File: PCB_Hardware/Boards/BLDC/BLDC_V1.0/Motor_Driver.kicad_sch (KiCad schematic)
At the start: 27 parts, among them J10 Conn_01x03_Pin, Q3 TPH3R70APL, Q4 TPH3R70APL, Q5 TPH3R70APL, Q6 TPH3R70APL, Q7 TPH3R70APL, Q8 TPH3R70APL, U1 DRV8353SRTAR

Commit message: Add DBcan transport refactor, BLDC V1.0 schematic + sim work, HAL submodule
- DBcan: replace bare-register driver with vendor-agnostic transport abstraction (core/, transports/, refactored bootloader driver, README)
- Add stm32g4xx_hal_driver as Firmware/libs submodule
- Add HAL config for BLDC board (stm32g4xx_hal_conf.h)
- BLDC V1.0: schematic edits across 10 sheets (footprint assignments, repositioning); design-doc README (gate-driver constraints, FET selection / TPH3R70APL, thermal analysis)
- ngspice simulation workflow (cap sweeps, half-bridge slow turn-on)
- Ignore .obsidian/ vault state and large simulation CSV exports
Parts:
- C15, C16: footprint (none) -> Capacitor_SMD:C_0603_1608Metric
- C17, C18, C19, C20, C21: footprint (none) -> Capacitor_SMD:C_0402_1005Metric
- C22, C25, C26, C27, C28: footprint (none) -> Capacitor_SMD:C_0805_2012Metric
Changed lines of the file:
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@@
 			)
 		)
-		(property "Footprint" ""
+		(property "Footprint" "Capacitor_SMD:C_0805_2012Metric"
 			(at 191.4652 40.64 0)
 			(hide yes)
@@
 			)
 		)
-		(property "Footprint" ""
+		(property "Footprint" "Capacitor_SMD:C_0603_1608Metric"
 			(at 110.1852 67.31 0)
 			(hide yes)
@@
 			)
 		)
-		(property "Footprint" ""
+		(property "Footprint" "Capacitor_SMD:C_0402_1005Metric"
 			(at 80.9752 97.79 0)
 			(hide yes)
@@
 			)
 		)
-		(property "Footprint" ""
+		(property "Footprint" "Capacitor_SMD:C_0402_1005Metric"
 			(at 135.5852 175.26 0)
 			(hide yes)
@@
 			)
 		)
-		(property "Footprint" ""
+		(property "Footprint" "Capacitor_SMD:C_0805_2012Metric"
 			(at 166.0652 40.64 0)
 			(hide yes)
@@
 			)
 		)
-		(property "Footprint" ""
+		(property "Footprint" "Capacitor_SMD:C_0805_2012Metric"
 			(at 153.3652 40.64 0)
 			(hide yes)
@@
 			)
 		)
-		(property "Footprint" ""
+		(property "Footprint" "Capacitor_SMD:C_0402_1005Metric"
 			(at 149.5552 175.26 0)
 			(hide yes)
@@
 			)
 		)
-		(property "Footprint" ""
+		(property "Footprint" "Capacitor_SMD:C_0603_1608Metric"
 			(at 110.1852 81.28 0)
 			(hide yes)
@@
 			)
 		)
-		(property "Footprint" ""
+		(property "Footprint" "Capacitor_SMD:C_0805_2012Metric"
 			(at 140.6652 40.64 0)
 			(hide yes)
@@
 			)
 		)
-		(property "Footprint" ""
+		(property "Footprint" "Capacitor_SMD:C_0805_2012Metric"
 			(at 178.7652 40.64 0)
 			(hide yes)
@@
 			)
 		)
-		(property "Footprint" ""
+		(property "Footprint" "Capacitor_SMD:C_0402_1005Metric"
 			(at 97.4852 64.77 0)
 			(hide yes)
@@
 			)
 		)
-		(property "Footprint" ""
+		(property "Footprint" "Capacitor_SMD:C_0402_1005Metric"
 			(at 92.4052 97.79 0)
 			(hide yes)

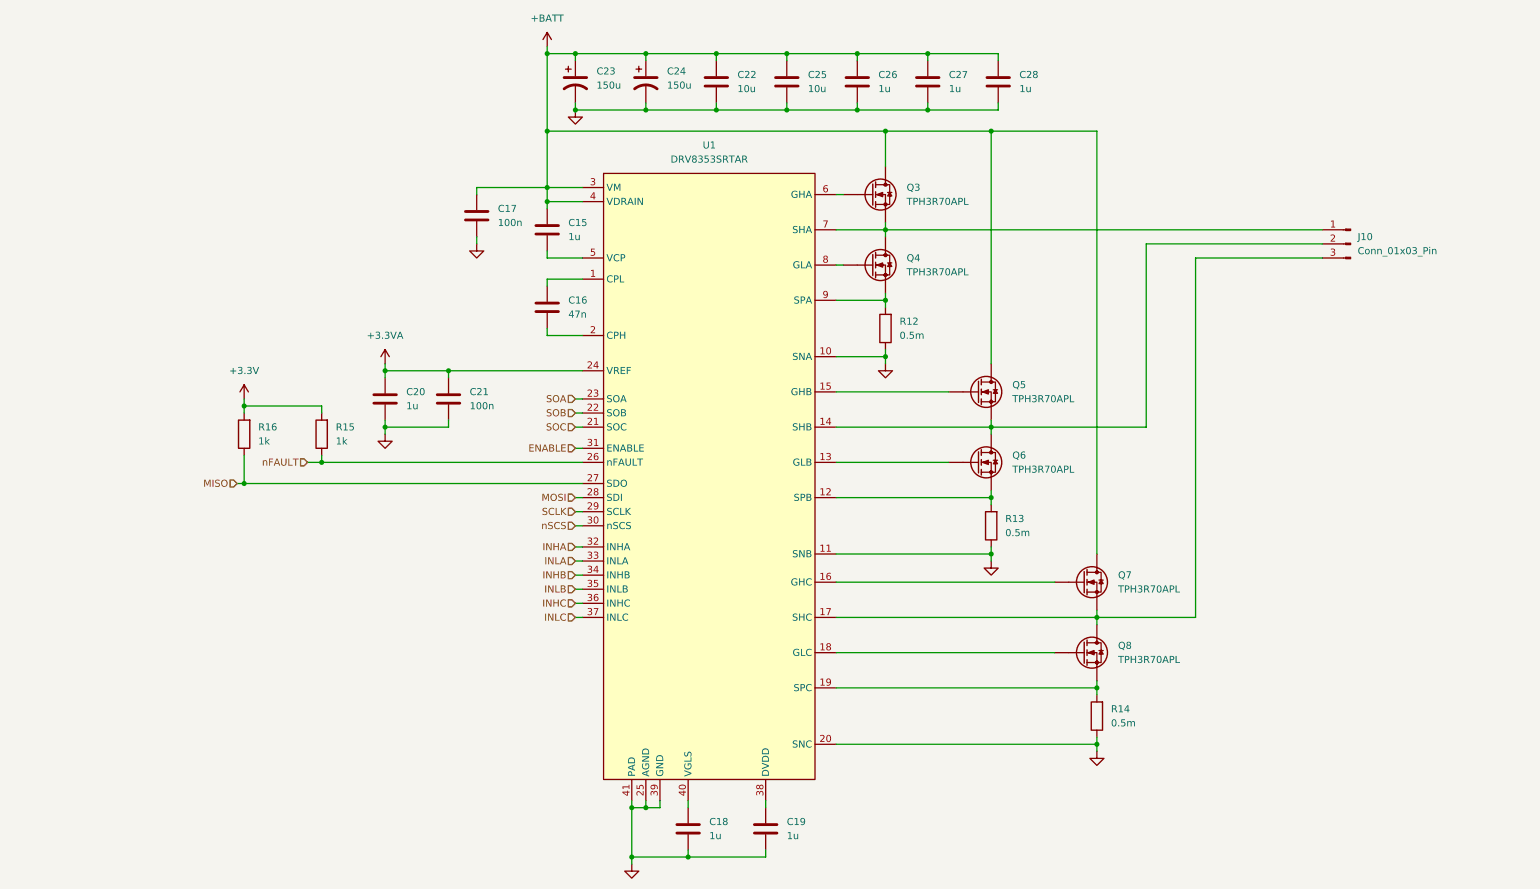
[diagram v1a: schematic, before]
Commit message: migrated claude skills to opencode, and added to the schematic review skill. Also updated the readme with calculations for the BLDC driver and changed the sense resistors to 1m Ohm
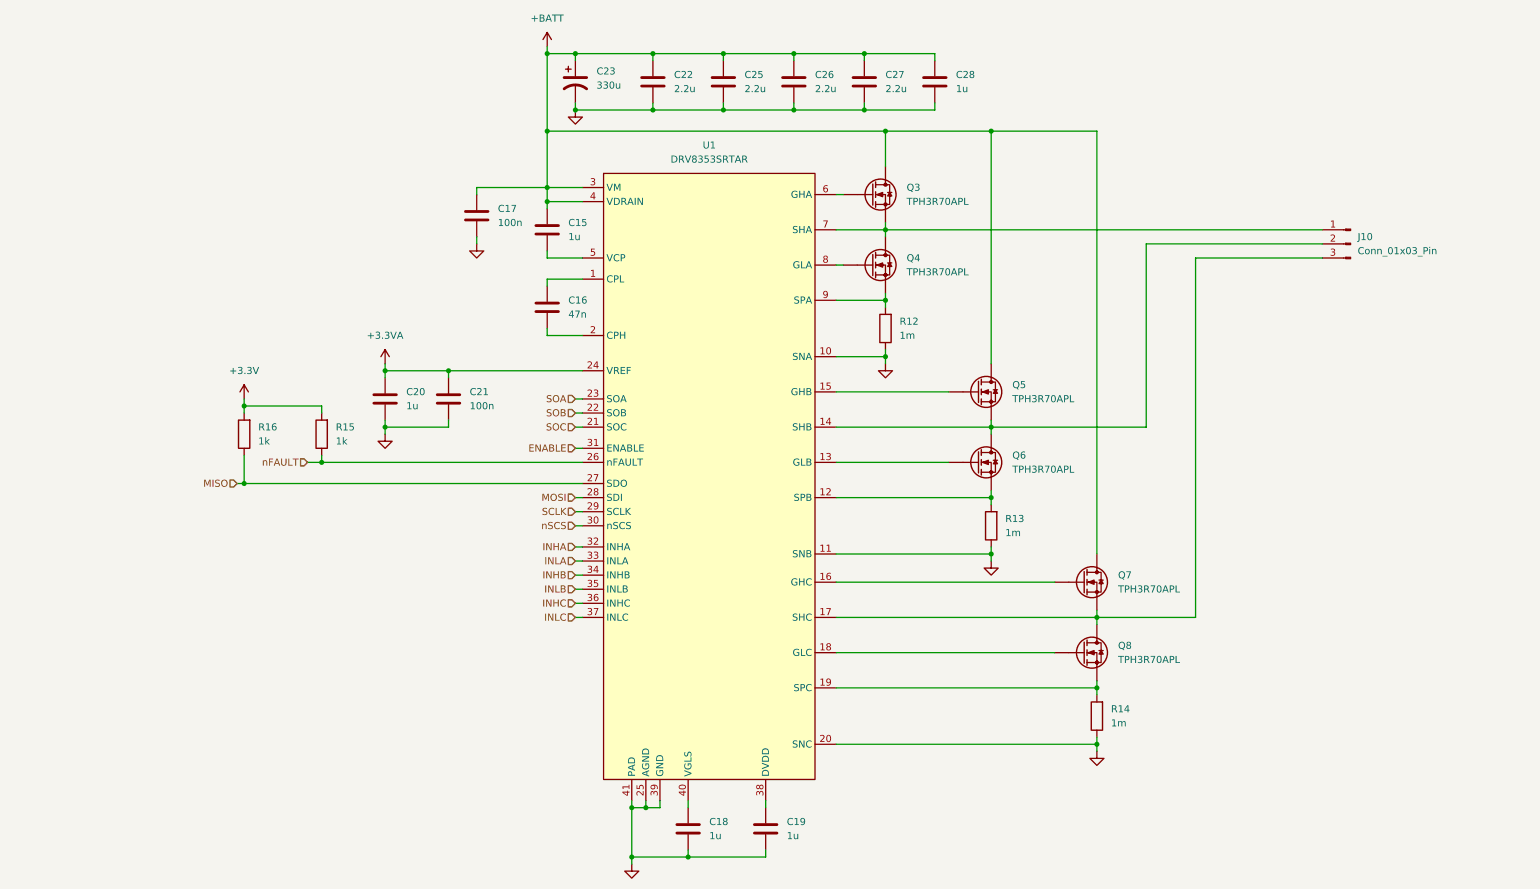
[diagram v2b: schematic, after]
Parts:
- removed C24: 150u, symbol Device:C_Polarized_US
- C22, C25: value 10u -> 2.2u
- C23: value 150u -> 330u
- C26, C27: value 1u -> 2.2u
- R12, R13, R14: value 0.5m -> 1m
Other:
- moved on the sheet: C22, C25, C26, C27, C28

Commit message: Created organization around the symbol lib and did a first pass layout of the BDLC
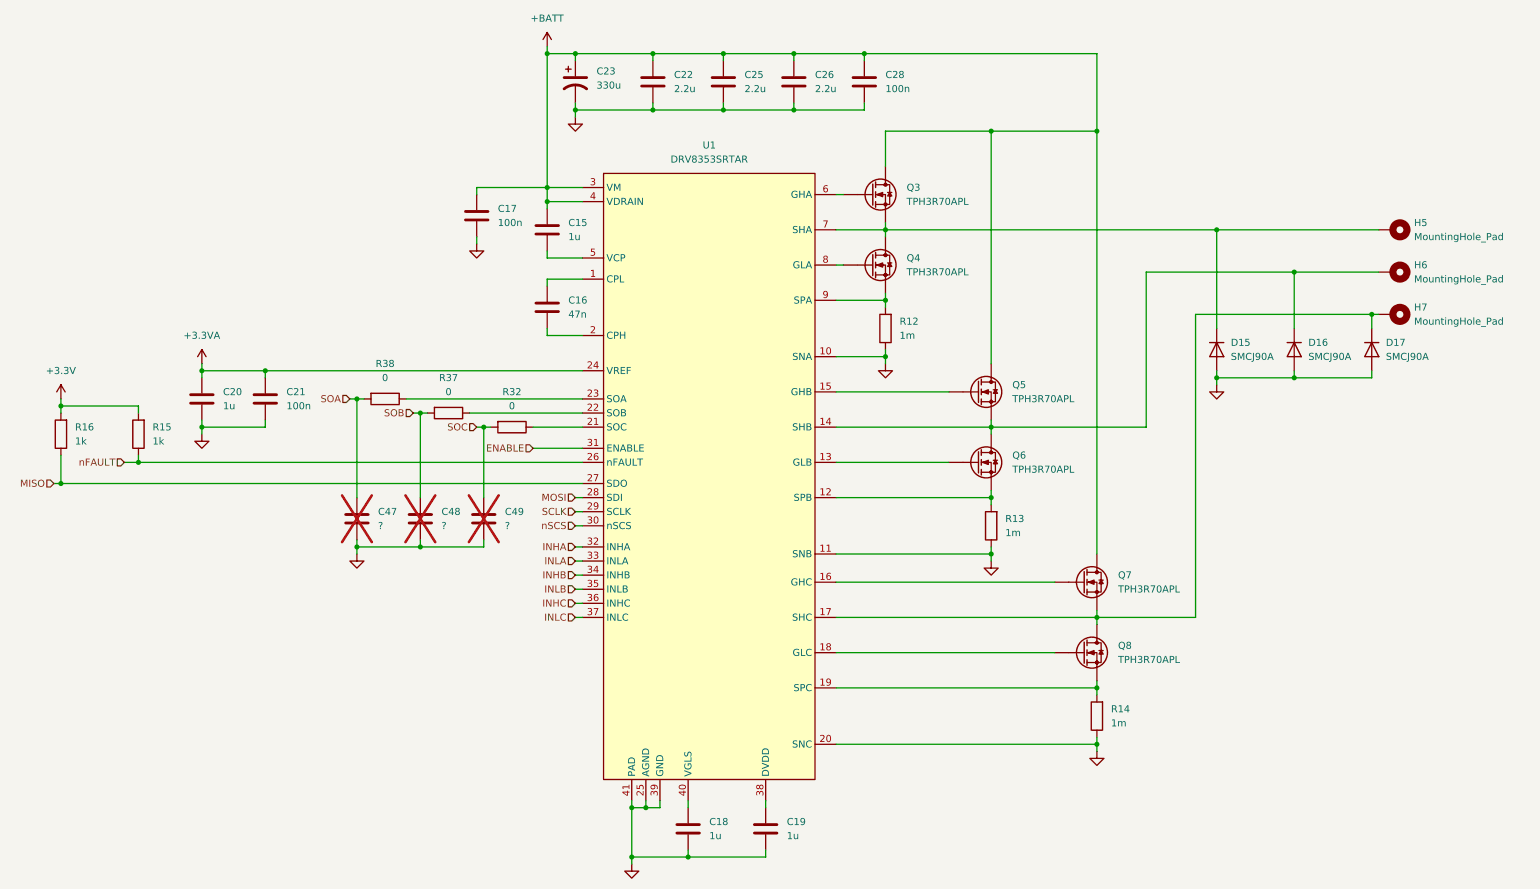
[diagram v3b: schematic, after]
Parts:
- removed C27: 2.2u, Capacitor_SMD:C_0805_2012Metric, symbol Device:C
- removed J10: Conn_01x03_Pin, symbol Connector:Conn_01x03_Pin
- added C47, C48, C49: ?, Capacitor_SMD:C_0402_1005Metric, symbol Device:C
- added D15, D16, D17: SMCJ90A, Diode_SMD:D_SMC, symbol Device:D
- added H5, H6, H7: MountingHole_Pad, MountingHole:MountingHole_3.2mm_M3_DIN965_Pad, symbol Mechanical:MountingHole_Pad
- added R32, R37, R38: 0, Resistor_SMD:R_0402_1005Metric, symbol Device:R
- C16: footprint Capacitor_SMD:C_0603_1608Metric -> Capacitor_SMD:C_0805_2012Metric
- C23: footprint (none) -> Capacitor_THT:CP_Radial_D12.5mm_P5.00mm
- C28: value 1u -> 100n
- Q3, Q4, Q5, Q6, Q7, Q8: footprint (none) -> DBRobot:SOP AdvanceN_TOS
- R15, R16: footprint Resistor_SMD:R_2512_6332Metric -> Resistor_SMD:R_0402_1005Metric
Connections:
- net GND: now also C47.2, C48.2, C49.2, D15.2 (A), D16.2 (A), D17.2 (A)
- net SOA: now also C47.1, R38.2; no longer U1.23 (SOA)
- net SOB: now also C48.1, R37.2; no longer U1.22 (SOB)
- net SOC: now also C49.1, R32.2; no longer U1.21 (SOC)
- net at Q7.1 (S), Q7.2 (S), Q7.3 (S)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: now also D17.1 (K), H7.1
- net at Q3.1 (S), Q3.2 (S), Q3.3 (S)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: now also D15.1 (K), H5.1
- net at Q5.1 (S), Q5.2 (S), Q5.3 (S)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: now also D16.1 (K), H6.1
- new net: R32.1, U1.21 (SOC)
- new net: R37.1, U1.22 (SOB)
- new net: R38.1, U1.23 (SOA)
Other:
- moved on the sheet: C20, C21, C28, R15, R16
